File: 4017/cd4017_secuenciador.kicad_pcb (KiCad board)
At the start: 2 copper layers, 91.8 x 47.2 mm, 24 parts, among them J1 CLK_IN_555, J2 ALIM_EXT, J3 POT1_EXT, J4 POT2_EXT, J5 POT3_EXT, J6 POT4_EXT, J7 JACK_OUT, U1 CD4017BE

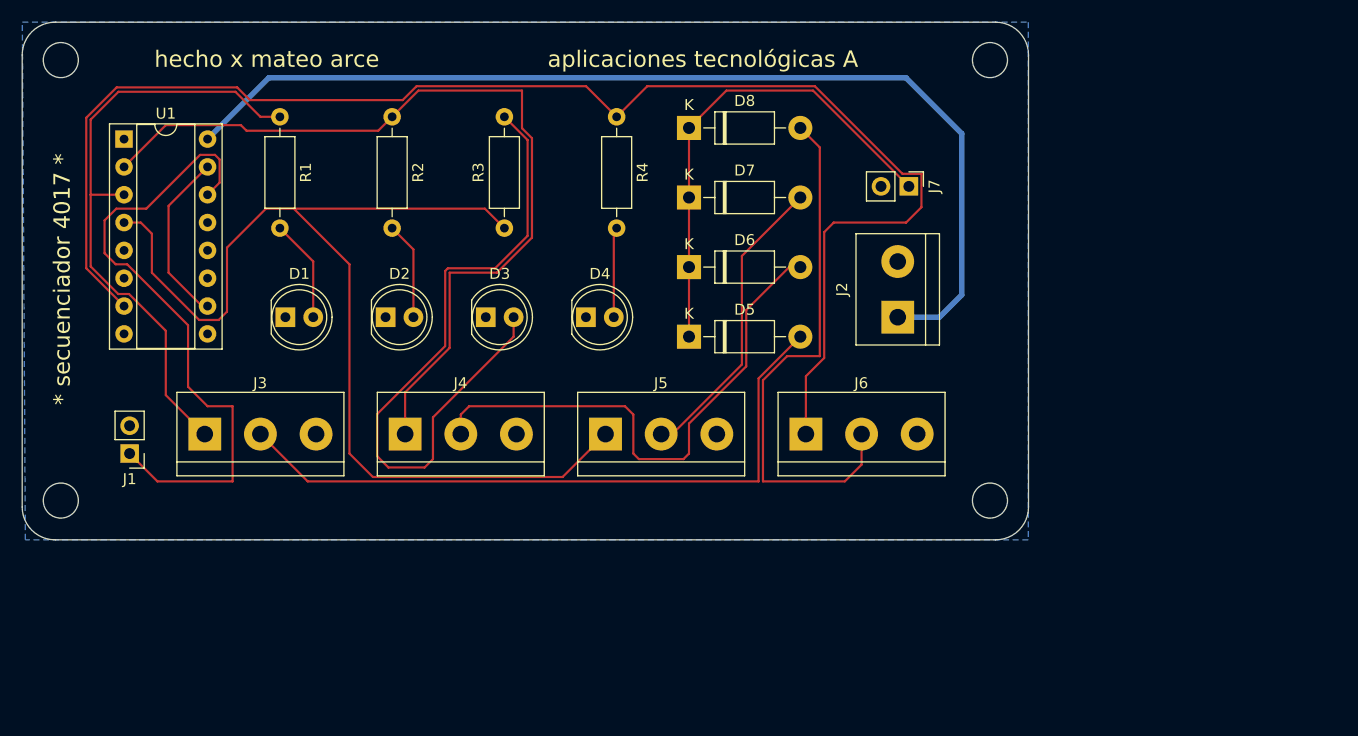
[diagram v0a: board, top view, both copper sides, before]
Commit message: fix 555 + design 4017
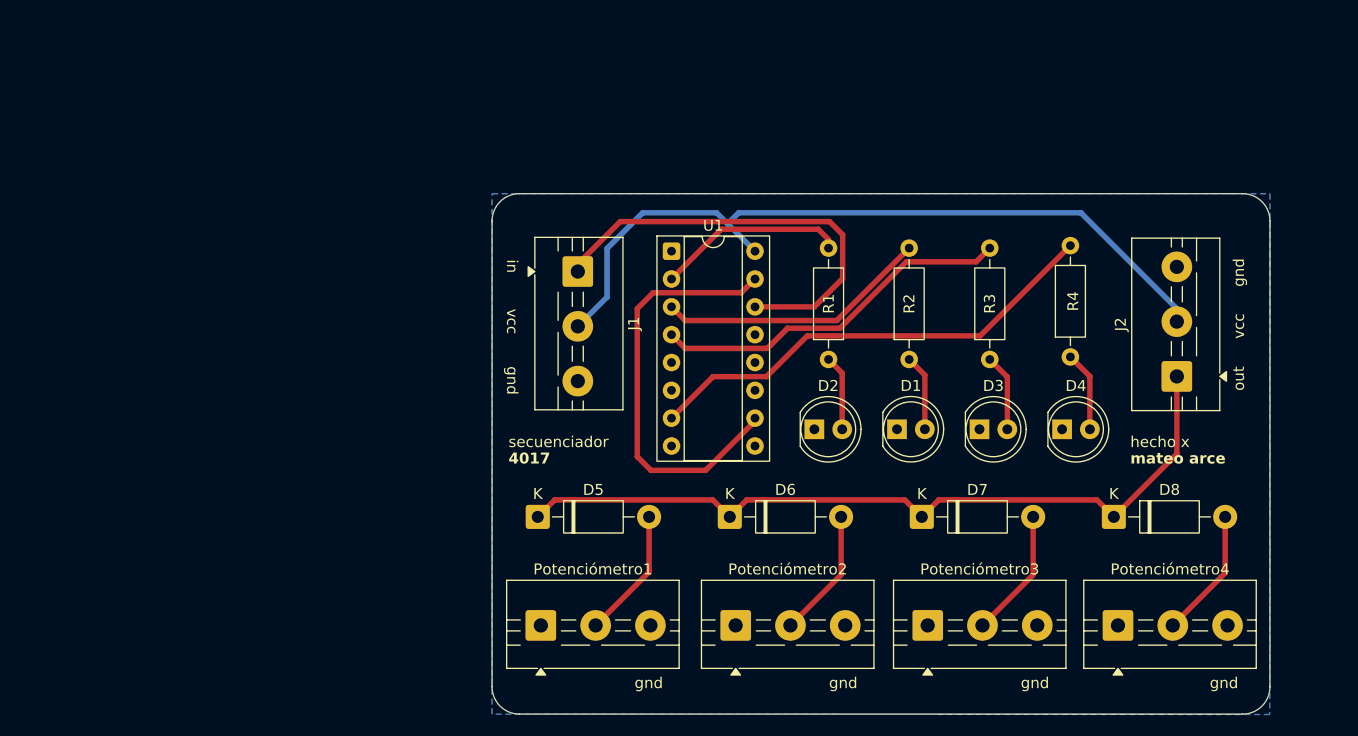
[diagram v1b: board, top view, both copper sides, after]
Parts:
- removed J3: POT1_EXT, TerminalBlock_bornier-3_P5.08mm
- removed J4: POT2_EXT, TerminalBlock_bornier-3_P5.08mm
- removed J5: POT3_EXT, TerminalBlock_bornier-3_P5.08mm
- removed J6: POT4_EXT, TerminalBlock_bornier-3_P5.08mm
- removed J7: JACK_OUT, PinHeader_1x02_P2.54mm_Vertical
- removed REF** (x4): MountingHole_3.2mm_M3, MountingHole:MountingHole_3.2mm_M3
- added Potenciómetro1: 100k, TerminalBlock:TerminalBlock_MaiXu_MX126-5.0-03P_1x03_P5.00mm, F.Cu at (144.5, 129.4)
- added Potenciómetro2: 100k, TerminalBlock:TerminalBlock_MaiXu_MX126-5.0-03P_1x03_P5.00mm, F.Cu at (162.2, 129.4)
- added Potenciómetro3: 100k, TerminalBlock:TerminalBlock_MaiXu_MX126-5.0-03P_1x03_P5.00mm, F.Cu at (179.8, 129.4)
- added Potenciómetro4: 100k, TerminalBlock:TerminalBlock_MaiXu_MX126-5.0-03P_1x03_P5.00mm, F.Cu at (197.1, 129.4)
- D1, D2, D3, D4: footprint LED_D5.0mm -> LED_THT:LED_D5.0mm
- D5, D6, D7, D8: value 1N4004 -> 1N4007; footprint D_DO-41_SOD81_P10.16mm_Horizontal -> Diode_THT:D_DO-41_SOD81_P10.16mm_Horizontal
- J1: value CLK_IN_555 -> Screw_Terminal_01x03; footprint PinHeader_1x02_P2.54mm_Vertical -> TerminalBlock:TerminalBlock_MaiXu_MX126-5.0-03P_1x03_P5.00mm
- J2: value ALIM_EXT -> Screw_Terminal_01x03; footprint TerminalBlock_bornier-2_P5.08mm -> TerminalBlock:TerminalBlock_MaiXu_MX126-5.0-03P_1x03_P5.00mm
- R1, R2, R3, R4: value 1k -> 10k; footprint R_Axial_DIN0207_L6.3mm_D2.5mm_P10.16mm_Horizontal -> Resistor_THT:R_Axial_DIN0207_L6.3mm_D2.5mm_P10.16mm_Horizontal
- U1: footprint DIP-16_W7.62mm_Socket -> Package_DIP:DIP-16_W7.62mm_Socket
- moved D1 56.7 mm to (177.0, 111.5)
- moved R1 54.8 mm to (170.7, 105.1), turned to 90 degrees
- moved D8 52.6 mm to (196.8, 119.5)
- moved R2 52.1 mm to (178.1, 105.1), turned to 90 degrees
- moved U1 51.0 mm to (156.4, 95.2)
- moved R4 46.9 mm to (192.8, 104.9), turned to 90 degrees
- moved D3 46.2 mm to (184.5, 111.5)
- moved R3 45.9 mm to (185.4, 105.1)
- moved D4 44.6 mm to (192.0, 111.5)
- moved J1 44.2 mm to (147.8, 97.1), turned to -90 degrees
- moved D2 40.4 mm to (169.4, 111.5)
- moved D7 36.1 mm to (179.2, 119.5)
- moved J2 26.0 mm to (202.5, 106.7)
- moved D6 23.1 mm to (161.7, 119.5)
- moved D5 21.5 mm to (144.2, 119.5)
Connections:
- net CLK_IN renamed Net-(J1-Pin_1)
- net Q4_RST renamed Net-(U1-Q4)
- D1 pad 2: Q0_LEDA -> Net-(D1-A)
- D2 pad 2: Q1_LEDA -> Net-(D2-A)
- D3 pad 2: Q2_LEDA -> Net-(D3-A)
- D4 pad 2: Q3_LEDA -> Net-(D4-A)
- D5 pad 1: MIX_OUT -> Net-(D5-K)
- D5 pad 2: Q0_WIPER -> Net-(D5-A)
- D6 pad 1: MIX_OUT -> Net-(D5-K)
- D6 pad 2: Q1_WIPER -> Net-(D6-A)
- D7 pad 1: MIX_OUT -> Net-(D5-K)
- D7 pad 2: Q2_WIPER -> Net-(D7-A)
- D8 pad 1: MIX_OUT -> Net-(D5-K)
- D8 pad 2: Q3_WIPER -> Net-(D8-A)
- J1 pad 2: GND -> VCC
- J2 pad 1: VCC -> Net-(D5-K)
- J2 pad 2: GND -> VCC
- R1 pad 1: Q0 -> Net-(D2-A)
- R1 pad 2: Q0_LEDA -> Net-(U1-Q1)
- R2 pad 1: Q1 -> Net-(D1-A)
- R2 pad 2: Q1_LEDA -> Net-(U1-Q0)
- R3 pad 1: Q2 -> Net-(D3-A)
- R3 pad 2: Q2_LEDA -> Net-(U1-Q2)
- R4 pad 1: Q3 -> Net-(D4-A)
- R4 pad 2: Q3_LEDA -> Net-(U1-Q3)
- U1 pad 1: (no net) -> unconnected-(U1-Q5-Pad1)
- U1 pad 11: (no net) -> unconnected-(U1-Q9-Pad11)
- U1 pad 12: (no net) -> unconnected-(U1-Cout-Pad12)
- U1 pad 2: Q1 -> Net-(U1-Q1)
- U1 pad 3: Q0 -> Net-(U1-Q0)
- U1 pad 4: Q2 -> Net-(U1-Q2)
- U1 pad 5: (no net) -> unconnected-(U1-Q6-Pad5)
- U1 pad 6: (no net) -> unconnected-(U1-Q7-Pad6)
- U1 pad 7: Q3 -> Net-(U1-Q3)
- U1 pad 9: (no net) -> unconnected-(U1-Q8-Pad9)
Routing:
- net Q3: track 134.6 -> 0.00 mm
- net Q2: track 99.2 -> 0.00 mm
- net Q1: track 78.7 -> 0.00 mm
- net Net-(D5-K): track 0.00 -> 71.6 mm
- net Q0_WIPER: track 62.0 -> 0.00 mm
- net Q2_LEDA: track 61.9 -> 0.00 mm
- net Q0: track 55.9 -> 0.00 mm
- net Q3_WIPER: track 49.3 -> 0.00 mm
- net Q1_WIPER: track 49.0 -> 0.00 mm
- net MIX_OUT: track 44.2 -> 0.00 mm
- net Net-(U1-Q3): track 0.00 -> 42.9 mm
- net Net-(U1-Q2): track 0.00 -> 33.4 mm
- net Q2_WIPER: track 27.4 -> 0.00 mm
- net Net-(U1-Q0): track 0.00 -> 24.9 mm
- net VCC: track 94.7 -> 70.7 mm
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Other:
- board size 91.8 x 47.2 mm -> 71 x 47.5 mm
- board text added: "4017"
- board text added: "gnd"
- board text added: "hecho x"
- board text added: "in"
- board text added: "mateo arce"
- board text added: "out"
- board text added: "secuenciador"
- board text added: "vcc"
- board text removed: "* secuenciador 4017 *"
- board text removed: "aplicaciones tecnológicas A"
- board text removed: "hecho x mateo arce"

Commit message: arreglar 4017 + iniciar 4093
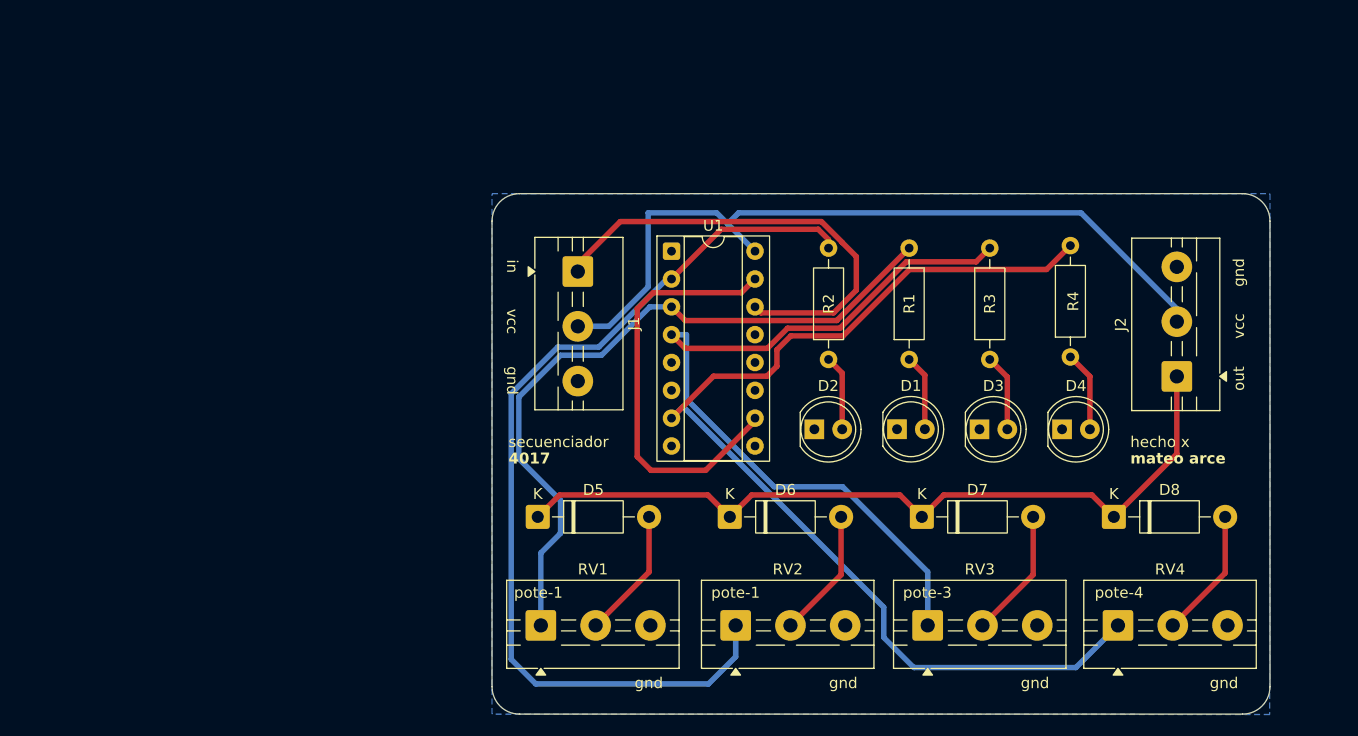
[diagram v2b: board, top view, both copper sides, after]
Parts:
- renumbered R2 to R1, R1 to R2, Potenciómetro1 to RV1, Potenciómetro2 to RV2, Potenciómetro3 to RV3, Potenciómetro4 to RV4
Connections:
- R1 pad 2: Net-(U1-Q0) -> /Q0
- R2 pad 2: Net-(U1-Q1) -> /Q1
- R3 pad 2: Net-(U1-Q2) -> /Q2
- R4 pad 2: Net-(U1-Q3) -> /Q3
- RV1 pad 1: /Q1 -> /Q0
- RV2 pad 1: /Q0 -> /Q1
- U1 pad 2: Net-(U1-Q1) -> /Q1
- U1 pad 3: Net-(U1-Q0) -> /Q0
- U1 pad 4: Net-(U1-Q2) -> /Q2
- U1 pad 7: Net-(U1-Q3) -> /Q3
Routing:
- net /Q3: track 0.00 -> 98.1 mm
- net /Q1: track 0.00 -> 85.9 mm
- net /Q2: track 0.00 -> 74.0 mm
- net /Q0: track 0.00 -> 65.5 mm
- net Net-(U1-Q3): track 42.9 -> 0.00 mm
- net Net-(U1-Q2): track 33.4 -> 0.00 mm
- net Net-(U1-Q0): track 24.9 -> 0.00 mm
- net Net-(U1-Q1): track 17.4 -> 0.00 mm
- net Net-(J1-Pin_1): track 40.0 -> 42.4 mm
- net VCC: track 70.7 -> 72.1 mm
- net Net-(D5-K): track 71.6 -> 72.8 mm
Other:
- board text added: "pote-1"
- board text added: "pote-3"
- board text added: "pote-4"

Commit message: gerbers + correcciones
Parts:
- added REF**: MountingHole_2.2mm_M2, MountingHole:MountingHole_2.2mm_M2, F.Cu at (150.0, 99.5)
- added REF**: MountingHole_2.2mm_M2, MountingHole:MountingHole_2.2mm_M2, F.Cu at (214.0, 99.5)
- moved R4 31.0 mm to (163.3, 114.5), turned to 0 degrees
- moved R1 29.0 mm to (149.6, 110.5), turned to 0 degrees
- moved D2 27.7 mm to (197.1, 112.8)
- moved R2 23.1 mm to (149.6, 114.5), turned to 0 degrees
- moved R3 22.7 mm to (163.3, 110.5), turned to 0 degrees
- moved U1 21.6 mm to (177.6, 99.1)
- moved D3 19.7 mm to (204.2, 112.8)
- moved D4 19.3 mm to (211.3, 112.8)
- moved J1 19.0 mm to (166.3, 101.5), turned to 180 degrees
- moved D1 13.1 mm to (190.0, 112.8)
- moved D5 7.27 mm to (151.1, 121.8)
- moved D6 7.25 mm to (168.6, 121.8)
- moved RV1 7.05 mm to (151.5, 129.7)
- moved J2 6.63 mm to (206.6, 101.5), turned to 180 degrees
- moved RV2 6.52 mm to (168.8, 129.7)
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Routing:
- net Net-(D2-A): track 6.89 -> 77.0 mm
- net Net-(D4-A): track 7.34 -> 74.4 mm
- net Net-(D1-A): track 6.96 -> 73.5 mm
- net /Q1: track 85.9 -> 44.8 mm
- net /Q2: track 74.0 -> 33.4 mm
- net Net-(D3-A): track 7.04 -> 45.4 mm
- net Net-(U1-Q4): track 38.8 -> 13.7 mm
- net VCC: track 72.1 -> 47.4 mm
- net /Q3: track 98.1 -> 75.0 mm
- net Net-(J1-Pin_1): track 42.4 -> 23.5 mm
- net /Q0: track 65.5 -> 55.1 mm
- net Net-(D5-K): track 72.8 -> 79.7 mm
- net Net-(D8-A): track 11.9 -> 9.97 mm
- net Net-(D7-A): track 11.8 -> 9.94 mm
- net Net-(D6-A): track 11.8 -> 10.0 mm
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- added copper zone on F.Cu, net GND
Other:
- board size 71 x 47.5 mm -> 70 x 38.2 mm
- board text added: "secuenciador 4017"
- board text removed: "4017"
- board text removed: "gnd"
- board text removed: "hecho x"
- board text removed: "in"
- board text removed: "mateo arce"
- board text removed: "out"
- board text removed: "pote-1"
- board text removed: "pote-3"
- board text removed: "pote-4"
- board text removed: "secuenciador"
- board text removed: "vcc"

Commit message: actualizar gerber
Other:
- board text added: "apliaciones tecnológicas A"
